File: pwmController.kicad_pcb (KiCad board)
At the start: 2 copper layers, 100 x 70 mm, 49 parts, among them J1 RJ12, J14 inputs, J16 relays, J17 relays, J5 power, J6 gnd, J7 inputs, J8 track out, K1 G5V-1, K2 G5V-1, K3 G5V-1, K4 G5V-1, K5 G5V-1, K6 G5V-1, K7 G5V-1, K8 G5V-1, U1 24LC256, U2 MAX485E, U3 L298N, U4 MCP23017_SP, U5 ULN2803A, U6 PCF8574, U7 Buck

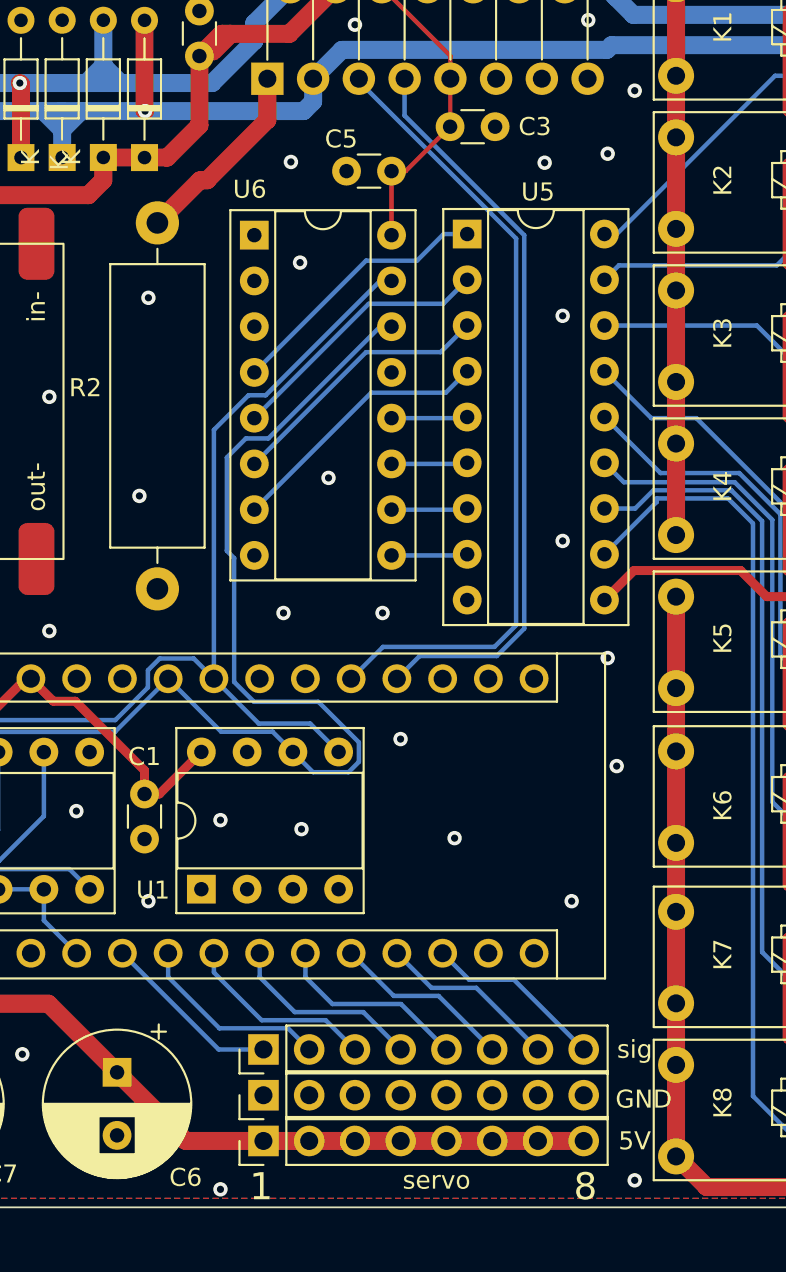
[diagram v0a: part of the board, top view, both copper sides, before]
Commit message: reading MCP works button debouncing works button reading works processing buttons, untested (need hardware for this) servoSweep works adjusting servos does not work (motors will not detach after an adjust) PWM controller works and is tested with 128 speed steps using z21, multimaus is untested. relays. No code for yet. shorcircuit, remains to be done (build in weistra control?)
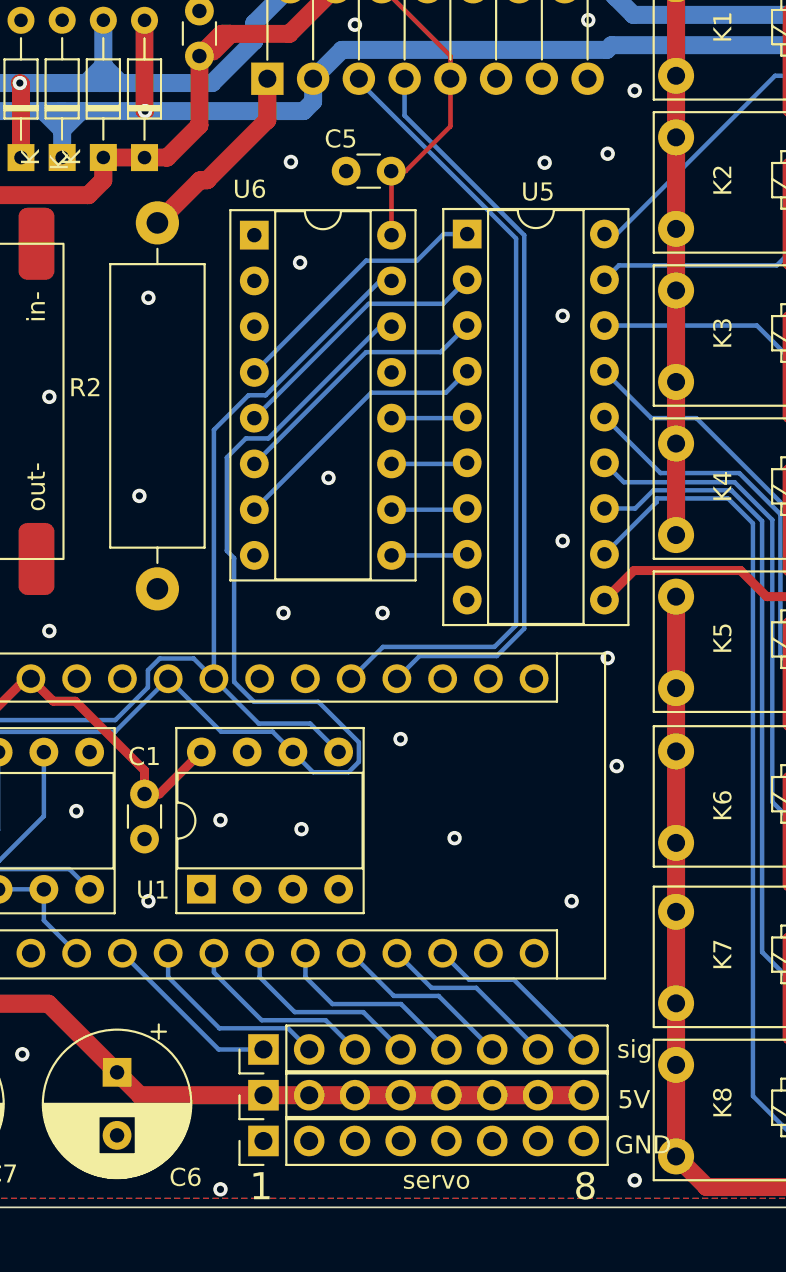
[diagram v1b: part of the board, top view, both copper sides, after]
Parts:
- removed C3: 100nF, Capacitor_THT:C_Disc_D3.0mm_W1.6mm_P2.50mm
- moved 5V 2.54 mm to (119.9, 96.8)
- moved GND 2.54 mm to (119.9, 99.3)
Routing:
- net +5VA: track 96.3 -> 95.2 mm
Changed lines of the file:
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@@
     (fp_line (start -1.4 -1.3) (end 6.4 -1.3) (layer "F.SilkS") (width 0.12))
     (fp_line (start 3.962 4.318) (end 3.327 4.318) (layer "F.SilkS") (width 0.12))
+    (fp_line (start 6.45 11.45) (end -1.45 11.45) (layer "F.CrtYd") (width 0.05))
     (fp_line (start -1.45 -1.35) (end -1.45 11.45) (layer "F.CrtYd") (width 0.05))
-    (fp_line (start 6.45 11.45) (end -1.45 11.45) (layer "F.CrtYd") (width 0.05))
     (fp_line (start 6.45 11.45) (end 6.45 -1.35) (layer "F.CrtYd") (width 0.05))
     (fp_line (start -1.45 -1.35) (end 6.45 -1.35) (layer "F.CrtYd") (width 0.05))
@@
   )
   (footprint "Capacitor_THT:C_Disc_D3.0mm_W1.6mm_P2.50mm" (layer "F.Cu")
-    (at 127 45.466 180)
+    (at 126.98 45.466 180)
     (descr "C, Disc series, Radial, pin pitch=2.50mm, , diameter*width=3.0*1.6mm^2, Capacitor, http://www.vishay.com/docs/45233/krseries.pdf")
     (tags "C Disc series Radial pin pitch 2.50mm  diameter 3.0mm width 1.6mm Capacitor")
@@
   )
   (footprint "Connector_PinHeader_2.54mm:PinHeader_1x08_P2.54mm_Vertical" (layer "F.Cu")
-    (at 119.888 99.314 90)
+    (at 119.888 96.774 90)
     (descr "Through hole straight pin header, 1x08, 2.54mm pitch, single row")
     (tags "Through hole pin header THT 1x08 2.54mm single row")
@@
     (property "Sheetname" "")
     (attr through_hole)
-    (fp_text reference "5V" (at 0 20.612 180) (layer "F.SilkS")
+    (fp_text reference "5V" (at -0.254 20.574 180) (layer "F.SilkS")
       (effects (font (size 1 1) (thickness 0.15)))
     )
@@
     (fp_line (start 3.911 -3.469) (end 3.911 -1.04) (layer "F.SilkS") (width 0.12))
     (fp_line (start 2.39 -4.03) (end 2.39 4.03) (layer "F.SilkS") (width 0.12))
+    (fp_line (start 4.511 1.04) (end 4.511 3.019) (layer "F.SilkS") (width 0.12))
     (fp_line (start 4.151 1.04) (end 4.151 3.309) (layer "F.SilkS") (width 0.12))
     (fp_line (start 2.07 -4.068) (end 2.07 4.068) (layer "F.SilkS") (width 0.12))
@@
     (fp_line (start 3.431 1.04) (end 3.431 3.722) (layer "F.SilkS") (width 0.12))
     (fp_line (start 2.511 1.04) (end 2.511 4.01) (layer "F.SilkS") (width 0.12))
-    (fp_line (start 4.511 1.04) (end 4.511 3.019) (layer "F.SilkS") (width 0.12))
     (fp_line (start 3.511 1.04) (end 3.511 3.686) (layer "F.SilkS") (width 0.12))
     (fp_line (start 3.631 1.04) (end 3.631 3.627) (layer "F.SilkS") (width 0.12))
@@
   )
   (footprint "Connector_PinHeader_2.54mm:PinHeader_1x08_P2.54mm_Vertical" (layer "F.Cu")
-    (at 119.888 96.774 90)
+    (at 119.888 99.314 90)
     (descr "Through hole straight pin header, 1x08, 2.54mm pitch, single row")
     (tags "Through hole pin header THT 1x08 2.54mm single row")
@@
     (property "Sheetname" "")
     (attr through_hole)
-    (fp_text reference "GND" (at -0.226 21.112 180) (layer "F.SilkS")
+    (fp_text reference "GND" (at -0.226 21.082 180) (layer "F.SilkS")
       (effects (font (size 1 1) (thickness 0.15)))
     )
@@
     (fp_circle (center 0 0) (end 3.45 0) (layer "F.CrtYd") (width 0.05) (fill none))
     (pad "" np_thru_hole circle (at 0 0) (size 3.2 3.2) (drill 3.2) (layers *.Cu *.Mask))
-  )
-  (footprint "Capacitor_THT:C_Disc_D3.0mm_W1.6mm_P2.50mm" (layer "F.Cu")
-    (at 130.25 43)
-    (descr "C, Disc series, Radial, pin pitch=2.50mm, , diameter*width=3.0*1.6mm^2, Capacitor, http://www.vishay.com/docs/45233/krseries.pdf")
-    (tags "C Disc series Radial pin pitch 2.50mm  diameter 3.0mm width 1.6mm Capacitor")
-    (property "Sheetfile" "pwmController.kicad_sch")
-    (property "Sheetname" "")
-    (attr through_hole)
-    (fp_text reference "C3" (at 4.71 0) (layer "F.SilkS")
-      (effects (font (size 1 1) (thickness 0.15)))
-    )
-    (fp_text value "100nF" (at 1.25 2.05) (layer "F.Fab")
-      (effects (font (size 1 1) (thickness 0.15)))
-    )
-    (fp_text user "${REFERENCE}" (at 1.25 0) (layer "F.Fab")
-      (effects (font (size 0.6 0.6) (thickness 0.09)))
-    )
-    (fp_line (start 0.621 -0.92) (end 1.879 -0.92) (layer "F.SilkS") (width 0.12))
-    (fp_line (start 0.621 0.92) (end 1.879 0.92) (layer "F.SilkS") (width 0.12))
-    (fp_line (start 3.55 -1.05) (end -1.05 -1.05) (layer "F.CrtYd") (width 0.05))
-    (fp_line (start -1.05 -1.05) (end -1.05 1.05) (layer "F.CrtYd") (width 0.05))
-    (fp_line (start 3.55 1.05) (end 3.55 -1.05) (layer "F.CrtYd") (width 0.05))
-    (fp_line (start -1.05 1.05) (end 3.55 1.05) (layer "F.CrtYd") (width 0.05))
-    (fp_line (start -0.25 0.8) (end 2.75 0.8) (layer "F.Fab") (width 0.1))
-    (fp_line (start 2.75 -0.8) (end -0.25 -0.8) (layer "F.Fab") (width 0.1))
-    (fp_line (start -0.25 -0.8) (end -0.25 0.8) (layer "F.Fab") (width 0.1))
-    (fp_line (start 2.75 0.8) (end 2.75 -0.8) (layer "F.Fab") (width 0.1))
-    (pad "1" thru_hole circle (at 0 0) (size 1.6 1.6) (drill 0.8) (layers *.Cu *.Mask)
-      (net 18 "+5V") (pintype "passive"))
-    (pad "2" thru_hole circle (at 2.5 0) (size 1.6 1.6) (drill 0.8) (layers *.Cu *.Mask)
-      (net 3 "GND") (pintype "passive"))
-    (model "${KICAD6_3DMODEL_DIR}/Capacitor_THT.3dshapes/C_Disc_D3.0mm_W1.6mm_P2.50mm.wrl"
-      (offset (xyz 0 0 0))
-      (scale (xyz 1 1 1))
-      (rotate (xyz 0 0 0))
-    )
   )
   (footprint "Diode_THT:D_DO-34_SOD68_P7.62mm_Horizontal" (layer "F.Cu")
@@
   (via (at 87.5 48) (size 0.8) (drill 0.4) (layers "F.Cu" "B.Cu") (free) (net 3))
   (via (at 95.5 93) (size 0.8) (drill 0.4) (layers "F.Cu" "B.Cu") (free) (net 3))
-  (via (at 127.5 77) (size 0.8) (drill 0.4) (layers "F.Cu" "B.Cu") (free) (net 3))
   (via (at 95 55.5) (size 0.8) (drill 0.4) (layers "F.Cu" "B.Cu") (free) (net 3))
   (via (at 103 81) (size 0.8) (drill 0.4) (layers "F.Cu" "B.Cu") (free) (net 3))
@@
   (via (at 103 36.5) (size 0.8) (drill 0.4) (layers "F.Cu" "B.Cu") (free) (net 3))
   (via (at 136.5 66) (size 0.8) (drill 0.4) (layers "F.Cu" "B.Cu") (free) (net 3))
-  (via (at 126.5 70) (size 0.8) (drill 0.4) (layers "F.Cu" "B.Cu") (free) (net 3))
   (via (at 140.5 41) (size 0.8) (drill 0.4) (layers "F.Cu" "B.Cu") (free) (net 3))
   (via (at 121.412 44.958) (size 0.8) (drill 0.4) (layers "F.Cu" "B.Cu") (free) (net 3))
@@
   (via (at 76.5 96.5) (size 0.8) (drill 0.4) (layers "F.Cu" "B.Cu") (free) (net 3))
   (via (at 123.5 62.5) (size 0.8) (drill 0.4) (layers "F.Cu" "B.Cu") (free) (net 3))
+  (via (at 127.5 77) (size 0.8) (drill 0.4) (layers "F.Cu" "B.Cu") (free) (net 3))
   (via (at 135.5 45) (size 0.8) (drill 0.4) (layers "F.Cu" "B.Cu") (free) (net 3))
   (via (at 121 70) (size 0.8) (drill 0.4) (layers "F.Cu" "B.Cu") (free) (net 3))
@@
   (via (at 103.5 65.5) (size 0.8) (drill 0.4) (layers "F.Cu" "B.Cu") (free) (net 3))
   (via (at 78 36) (size 0.8) (drill 0.4) (layers "F.Cu" "B.Cu") (free) (net 3))
+  (via (at 126.5 70) (size 0.8) (drill 0.4) (layers "F.Cu" "B.Cu") (free) (net 3))
   (via (at 139 72.5) (size 0.8) (drill 0.4) (layers "F.Cu" "B.Cu") (free) (net 3))
   (via (at 93.5 67.5) (size 0.8) (drill 0.4) (layers "F.Cu" "B.Cu") (free) (net 3))
@@
   (segment (start 156.21 35.306) (end 156.718 35.306) (width 0.5) (layer "B.Cu") (net 19))
   (segment (start 111.76 95.504) (end 107.95 91.694) (width 1) (layer "F.Cu") (net 20))
-  (segment (start 115.57 99.314) (end 111.76 95.504) (width 1) (layer "F.Cu") (net 20))
-  (segment (start 119.888 99.314) (end 115.57 99.314) (width 1) (layer "F.Cu") (net 20))
+  (segment (start 111.76 95.504) (end 113.03 96.774) (width 1) (layer "F.Cu") (net 20))
   (segment (start 98.298 67.012) (end 98.286 67) (width 1) (layer "F.Cu") (net 20))
+  (segment (start 119.888 96.774) (end 137.668 96.774) (width 1) (layer "F.Cu") (net 20))
   (segment (start 96.774 89.916) (end 96.774 71.882) (width 1) (layer "F.Cu") (net 20))
-  (segment (start 137.668 99.314) (end 119.888 99.314) (width 1) (layer "F.Cu") (net 20))
   (segment (start 99.766 67) (end 98.286 67) (width 0.5) (layer "F.Cu") (net 20))
   (segment (start 100.584 70.104) (end 100.584 67.818) (width 0.5) (layer "F.Cu") (net 20))
@@
   (segment (start 96.774 71.882) (end 98.298 70.358) (width 1) (layer "F.Cu") (net 20))
   (segment (start 98.298 70.358) (end 98.298 67.012) (width 1) (layer "F.Cu") (net 20))
+  (segment (start 113.03 96.774) (end 119.888 96.774) (width 1) (layer "F.Cu") (net 20))
   (segment (start 107.95 91.694) (end 98.552 91.694) (width 1) (layer "F.Cu") (net 20))
   (segment (start 100.584 67.818) (end 99.766 67) (width 0.5) (layer "F.Cu") (net 20))

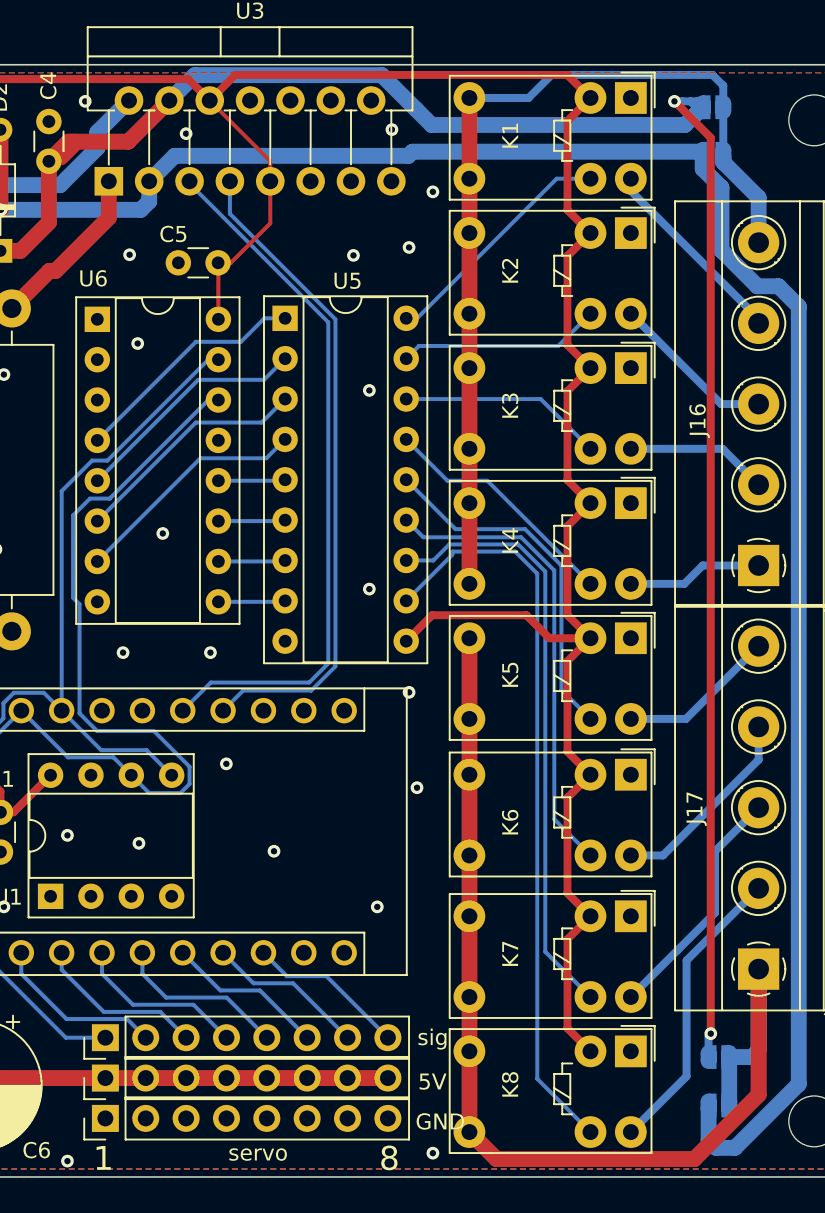
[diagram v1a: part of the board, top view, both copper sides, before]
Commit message: may have the relays working. Should be tested with an LED as soon as the IO extender arrives. Also need to solder pin1 (A0) to 5V due to address conflict with mcp23017
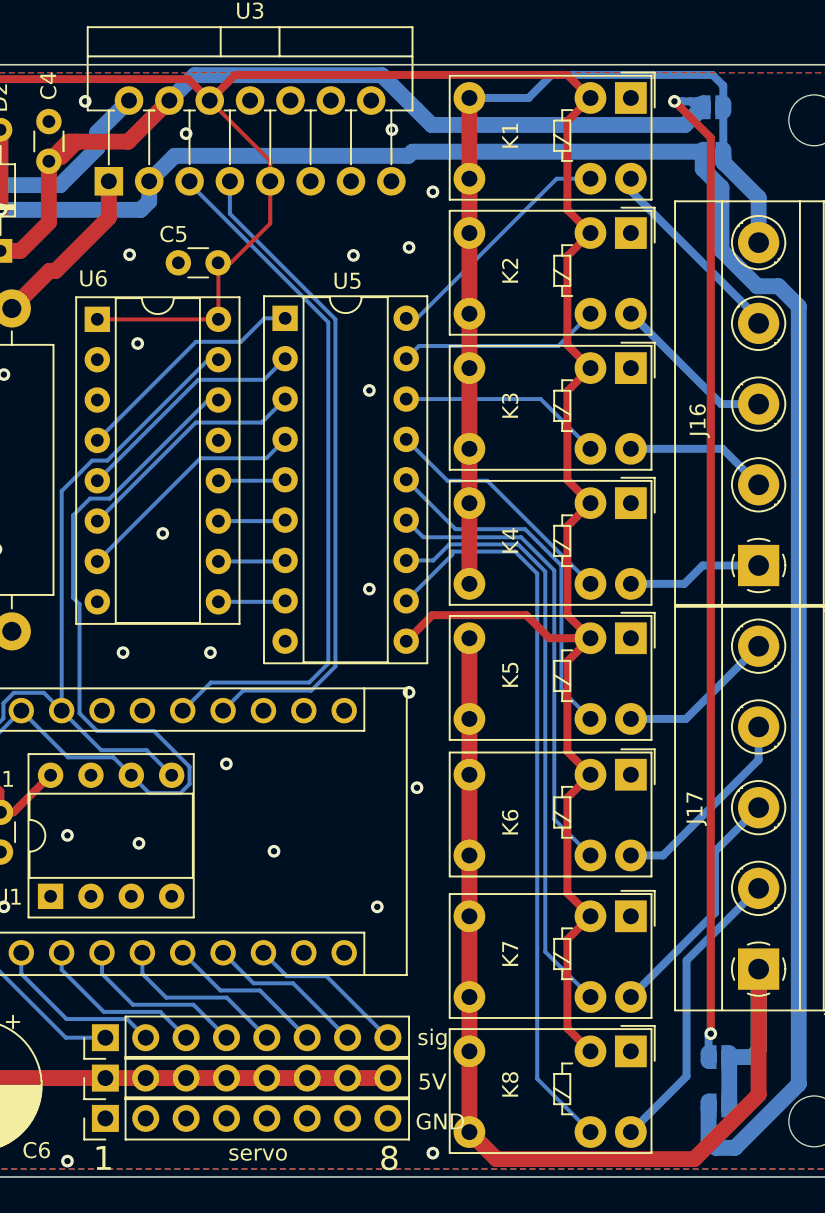
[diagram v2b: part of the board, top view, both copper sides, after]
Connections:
- U6 pad 1: GND -> +5V
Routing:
- net +5V: track 288.6 -> 296.2 mm
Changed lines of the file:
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@@
   (net 98 "unconnected-(U4-Pad20)")
   (net 99 "unconnected-(U6-Pad13)")
-  (net 100 "Net-(J5-Pad1)")
+  (net 100 "Net-(D7-Pad2)")
   (footprint "Diode_THT:D_DO-34_SOD68_P7.62mm_Horizontal" (layer "F.Cu")
     (at 91.948 59.441 90)
@@
     (fp_circle (center 0 0) (end 1.5 0) (layer "F.Fab") (width 0.1) (fill none))
     (pad "1" thru_hole rect (at 0 0 180) (size 2.6 2.6) (drill 1.3) (layers *.Cu *.Mask)
-      (net 100 "Net-(J5-Pad1)") (pinfunction "Pin_1") (pintype "passive"))
+      (net 100 "Net-(D7-Pad2)") (pinfunction "Pin_1") (pintype "passive"))
     (pad "2" thru_hole circle (at 5.08 0 180) (size 2.6 2.6) (drill 1.3) (layers *.Cu *.Mask)
       (net 3 "GND") (pinfunction "Pin_2") (pintype "passive"))
@@
     (fp_line (start -1.27 19.11) (end 8.89 19.11) (layer "F.Fab") (width 0.1))
     (pad "1" thru_hole rect (at 0 0) (size 1.6 1.6) (drill 0.8) (layers *.Cu *.Mask)
-      (net 3 "GND") (pinfunction "A0") (pintype "input"))
+      (net 18 "+5V") (pinfunction "A0") (pintype "input"))
     (pad "2" thru_hole oval (at 0 2.54) (size 1.6 1.6) (drill 0.8) (layers *.Cu *.Mask)
       (net 3 "GND") (pinfunction "A1") (pintype "input"))
@@
       (net 19 "+12V") (pinfunction "K") (pintype "passive"))
     (pad "2" thru_hole oval (at 7.62 0 90) (size 1.5 1.5) (drill 0.75) (layers *.Cu *.Mask)
-      (net 100 "Net-(J5-Pad1)") (pinfunction "A") (pintype "passive"))
+      (net 100 "Net-(D7-Pad2)") (pinfunction "A") (pintype "passive"))
     (model "${KICAD6_3DMODEL_DIR}/Diode_THT.3dshapes/D_DO-34_SOD68_P7.62mm_Horizontal.wrl"
       (offset (xyz 0 0 0))
@@
         (gr_circle (center 0 0.25) (end 0.5 0.25) (width 0) (fill yes))
         (gr_poly (pts
-            (xy 0.5 -0.75)
-            (xy 0 -0.75)
-            (xy 0 0.75)
             (xy 0.5 0.75)
+            (xy 0 0.75)
+            (xy 0 -0.75)
+            (xy 0.5 -0.75)
           ) (width 0) (fill yes))
       ))
@@
         (gr_circle (center 0 0.25) (end 0.5 0.25) (width 0) (fill yes))
         (gr_poly (pts
-            (xy 0 -0.75)
-            (xy -0.5 -0.75)
-            (xy -0.5 0.75)
             (xy 0 0.75)
+            (xy -0.5 0.75)
+            (xy -0.5 -0.75)
+            (xy 0 -0.75)
           ) (width 0) (fill yes))
       ))
@@
         (gr_circle (center 0 0.25) (end 0.5 0.25) (width 0) (fill yes))
         (gr_poly (pts
-            (xy 0.5 -0.75)
-            (xy 0 -0.75)
-            (xy 0 0.75)
             (xy 0.5 0.75)
+            (xy 0 0.75)
+            (xy 0 -0.75)
+            (xy 0.5 -0.75)
           ) (width 0) (fill yes))
       ))
@@
         (gr_circle (center 0 0.25) (end 0.5 0.25) (width 0) (fill yes))
         (gr_poly (pts
-            (xy 0 -0.75)
-            (xy -0.5 -0.75)
-            (xy -0.5 0.75)
             (xy 0 0.75)
+            (xy -0.5 0.75)
+            (xy -0.5 -0.75)
+            (xy 0 -0.75)
           ) (width 0) (fill yes))
       ))
@@
         (gr_circle (center 0 0.25) (end 0.5 0.25) (width 0) (fill yes))
         (gr_poly (pts
-            (xy 0.5 -0.75)
-            (xy 0 -0.75)
-            (xy 0 0.75)
             (xy 0.5 0.75)
+            (xy 0 0.75)
+            (xy 0 -0.75)
+            (xy 0.5 -0.75)
           ) (width 0) (fill yes))
       ))
@@
         (gr_circle (center 0 0.25) (end 0.5 0.25) (width 0) (fill yes))
         (gr_poly (pts
-            (xy 0 -0.75)
-            (xy -0.5 -0.75)
-            (xy -0.5 0.75)
             (xy 0 0.75)
+            (xy -0.5 0.75)
+            (xy -0.5 -0.75)
+            (xy 0 -0.75)
           ) (width 0) (fill yes))
       ))
@@
         (gr_circle (center 0 0.25) (end 0.5 0.25) (width 0) (fill yes))
         (gr_poly (pts
-            (xy 0.5 -0.75)
-            (xy 0 -0.75)
-            (xy 0 0.75)
             (xy 0.5 0.75)
+            (xy 0 0.75)
+            (xy 0 -0.75)
+            (xy 0.5 -0.75)
           ) (width 0) (fill yes))
       ))
@@
         (gr_circle (center 0 0.25) (end 0.5 0.25) (width 0) (fill yes))
         (gr_poly (pts
-            (xy 0 -0.75)
-            (xy -0.5 -0.75)
-            (xy -0.5 0.75)
             (xy 0 0.75)
+            (xy -0.5 0.75)
+            (xy -0.5 -0.75)
+            (xy 0 -0.75)
           ) (width 0) (fill yes))
       ))
@@
     (pts (xy 168 103) (xy 68 103))
     (height -8.5)
-    (gr_text "100.0000 mm" (at 118 110.35) (layer "Dwgs.User")
+    (gr_text "100,0000 mm" (at 118 110.35) (layer "Dwgs.User")
       (effects (font (size 1 1) (thickness 0.15)))
     )
@@
     (pts (xy 68 103) (xy 68 33))
     (height -15.5)
-    (gr_text "70.0000 mm" (at 51.35 68 90) (layer "Dwgs.User")
+    (gr_text "70,0000 mm" (at 51.35 68 90) (layer "Dwgs.User")
       (effects (font (size 1 1) (thickness 0.15)))
     )
@@
   (segment (start 138.82 69.28) (end 140.457011 67.642989) (width 0.5) (layer "F.Cu") (net 18))
   (segment (start 91.948 59.441) (end 91.948 74.608) (width 0.5) (layer "F.Cu") (net 18))
+  (segment (start 119.38 49.022) (end 127 49.022) (width 0.25) (layer "F.Cu") (net 18))
   (segment (start 97.204 77.9) (end 99.314 80.01) (width 0.5) (layer "B.Cu") (net 18))
   (segment (start 88.656 77.9) (end 97.204 77.9) (width 0.5) (layer "B.Cu") (net 18))
